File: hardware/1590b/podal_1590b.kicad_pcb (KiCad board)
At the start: 2 copper layers, 54 x 60 mm, 52 parts, among them J3 fsw pin 2, J4 fsw pin 4, J5 fsw pin 5, J8 Right out, J9 fsw pin 3, SW1 Switch 1, SW2 Switch 2, SW3 RotaryEncoder_Switch, U1 TL074, U2 L78L05_TO92

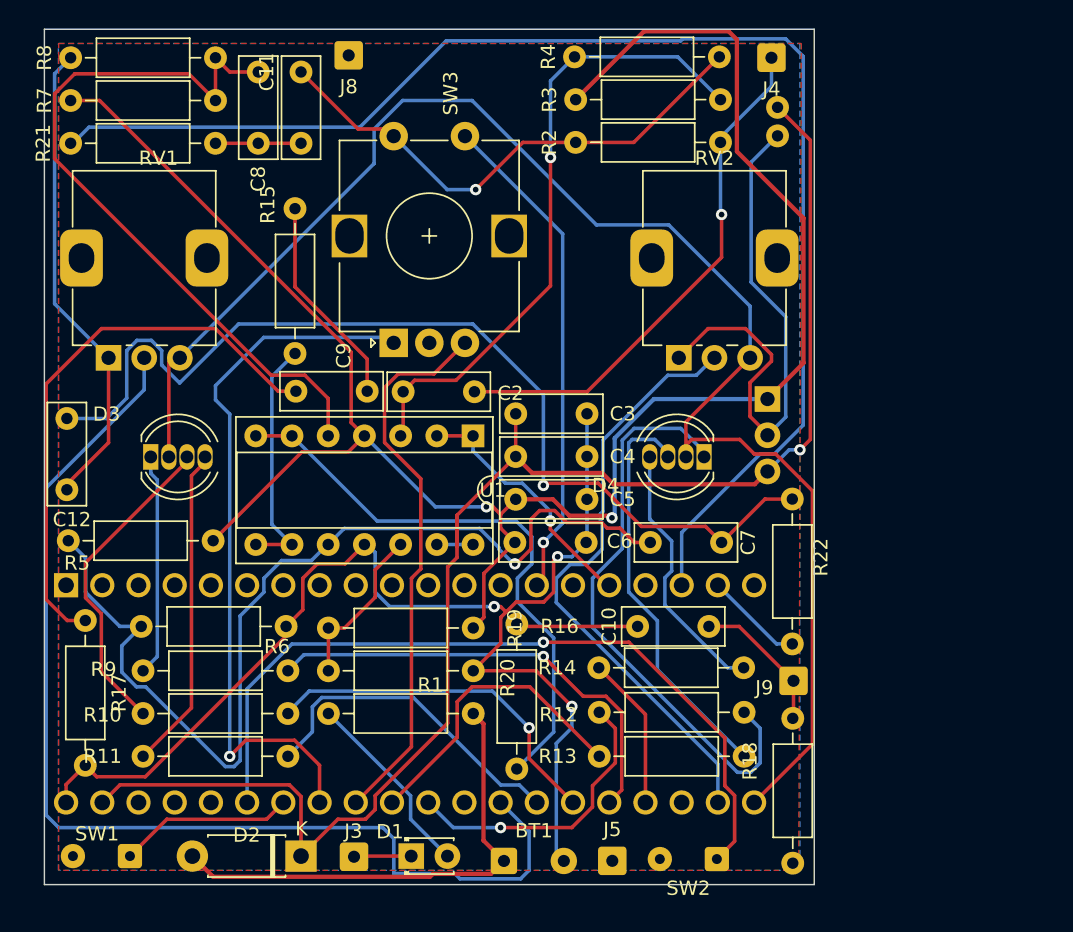
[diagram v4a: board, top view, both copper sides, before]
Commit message: Reorganise hardware into enclosure size
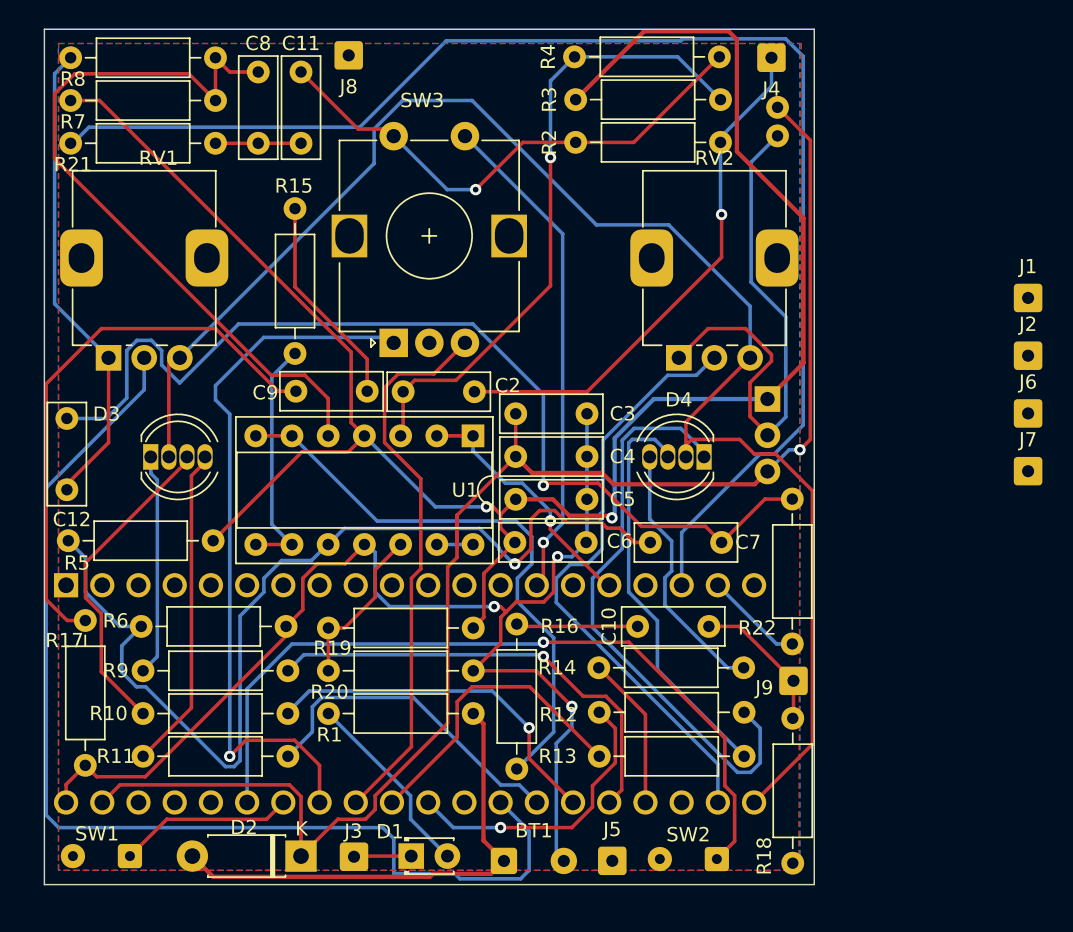
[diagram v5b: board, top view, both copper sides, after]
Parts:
- added J1: Guitar in, Connector_Wire:SolderWire-0.25sqmm_1x01_D0.65mm_OD2mm, F.Cu at (169.0, 68.8)
- added J2: fsw pin 1, Connector_Wire:SolderWire-0.25sqmm_1x01_D0.65mm_OD2mm, F.Cu at (169.0, 72.9)
- added J6: fsw pin 6, Connector_Wire:SolderWire-0.25sqmm_1x01_D0.65mm_OD2mm, F.Cu at (169.0, 77.0)
- added J7: Left out, Connector_Wire:SolderWire-0.25sqmm_1x01_D0.65mm_OD2mm, F.Cu at (169.0, 81.0)

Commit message: Tidy up pcb and compressor
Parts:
- removed J1: Guitar in, Connector_Wire:SolderWire-0.25sqmm_1x01_D0.65mm_OD2mm
- removed J2: fsw pin 1, Connector_Wire:SolderWire-0.25sqmm_1x01_D0.65mm_OD2mm
- removed J6: fsw pin 6, Connector_Wire:SolderWire-0.25sqmm_1x01_D0.65mm_OD2mm
- removed J7: Left out, Connector_Wire:SolderWire-0.25sqmm_1x01_D0.65mm_OD2mm
- moved C10 0.24 mm to (141.8, 91.7)
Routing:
- net /VCC: track 106.6 -> 104.4 mm
- net Net-(D4-RK): track 41.4 -> 42.8 mm
- net Net-(U1B-+): track 52.4 -> 53.1 mm
- net Net-(U1C-+): track 71.4 -> 72.0 mm
- net Net-(A1-ADC_0): track 42.5 -> 43.1 mm
- net Net-(D4-GK): track 28.9 -> 29.4 mm
- net Net-(A1-SAI2_SD_A): track 51.5 -> 52.0 mm

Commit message: Add footprint for the LM7805
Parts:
- U2: footprint Package_TO_SOT_THT:TO-92_Inline_Wide_78L05_dc -> Library:TO-92_Inline_Wide_78L05_dc
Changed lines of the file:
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@@
 		)
 	)
-	(footprint "Package_TO_SOT_THT:TO-92_Inline_Wide_78L05_dc"
+	(footprint "Library:TO-92_Inline_Wide_78L05_dc"
 		(layer "B.Cu")
 		(at 150.720433 75.940131 -90)
@@
 		(tags "to-92 sc-43 sc-43a sot54 PA33 transistor")
 		(property "Reference" "U2"
-			(at -0.440131 -2.279567 90)
+			(at 2.54 3.56 -90)
 			(layer "B.SilkS")
 			(effects
@@
 		)
 		(property "Value" "L78L05_TO92"
-			(at 2.54 -2.79 90)
+			(at 2.54 -2.79 -90)
 			(layer "B.Fab")
 			(effects
@@
 			)
 		)
-		(property "Footprint" "Package_TO_SOT_THT:TO-92_Inline_Wide_78L05_dc"
-			(at 0 0 -90)
+		(property "Footprint" "Library:TO-92_Inline_Wide_78L05_dc"
+			(at 0 0 90)
 			(unlocked yes)
-			(layer "F.Fab")
+			(layer "B.Fab")
 			(hide yes)
 			(effects
@@
 					(size 1.27 1.27)
 				)
+				(justify mirror)
 			)
 		)
 		(property "Datasheet" "http://www.st.com/content/ccc/resource/technical/document/datasheet/15/55/e5/aa/23/5b/43/fd/CD00000446.pdf/files/CD00000446.pdf/jcr:content/translations/en.CD00000446.pdf"
-			(at 0 0 -90)
+			(at 0 0 90)
 			(unlocked yes)
-			(layer "F.Fab")
+			(layer "B.Fab")
 			(hide yes)
 			(effects
@@
 					(size 1.27 1.27)
 				)
+				(justify mirror)
 			)
 		)
 		(property "Description" ""
-			(at 0 0 -90)
+			(at 0 0 90)
 			(unlocked yes)
-			(layer "F.Fab")
+			(layer "B.Fab")
 			(hide yes)
 			(effects
@@
 					(size 1.27 1.27)
 				)
+				(justify mirror)
 			)
 		)
@@
 		(attr through_hole)
 		(fp_line
-			(start 0.74 -1.85)
-			(end 4.34 -1.85)
+			(start 4.34 -1.85)
+			(end 0.74 -1.85)
 			(stroke
 				(width 0.12)
@@
 		)
 		(fp_line
-			(start -1.01 2.73)
-			(end 6.09 2.73)
+			(start 6.09 2.73)
+			(end -1.01 2.73)
 			(stroke
 				(width 0.05)
@@
 		)
 		(fp_line
-			(start -1.01 2.73)
-			(end -1.01 -2.01)
+			(start 6.09 2.73)
+			(end 6.09 -2.01)
 			(stroke
 				(width 0.05)
@@
 		)
 		(fp_line
-			(start 6.09 -2.01)
-			(end 6.09 2.73)
+			(start -1.01 -2.01)
+			(end -1.01 2.73)
 			(stroke
 				(width 0.05)
@@
 		)
 		(fp_line
-			(start 6.09 -2.01)
-			(end -1.01 -2.01)
+			(start -1.01 -2.01)
+			(end 6.09 -2.01)
 			(stroke
 				(width 0.05)
@@
 		)
 		(fp_line
-			(start 0.8 -1.75)
-			(end 4.3 -1.75)
+			(start 4.3 -1.75)
+			(end 0.8 -1.75)
 			(stroke
 				(width 0.1)
@@
 		)
 		(fp_text user "${REFERENCE}"
-			(at 2.54 0 90)
+			(at 2.54 0 -90)
 			(layer "B.Fab")
 			(effects

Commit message: Fix Red and blue LEDs - were the wrong way round
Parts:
- added J1: Guitar in, Connector_Wire:SolderWire-0.25sqmm_1x01_D0.65mm_OD2mm, F.Cu at (1.77, 1.52)
- added J2: fsw pin 1, Connector_Wire:SolderWire-0.25sqmm_1x01_D0.65mm_OD2mm, F.Cu at (1.77, 5.58)
- added J6: fsw pin 6, Connector_Wire:SolderWire-0.25sqmm_1x01_D0.65mm_OD2mm, F.Cu at (1.77, 9.62)
- added J7: Left out, Connector_Wire:SolderWire-0.25sqmm_1x01_D0.65mm_OD2mm, F.Cu at (1.77, 13.7)
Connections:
- R11 pad 1: /LED_1_R -> /LED_1_B
- R12 pad 1: /LED_2_B -> /LED_2_R
- R14 pad 1: /LED_2_R -> /LED_2_B
- R9 pad 1: /LED_1_B -> /LED_1_R
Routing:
- net /LED_2_B: track 20.6 -> 26.1 mm
- net /LED_1_B: track 32.7 -> 28.3 mm
- net /LED_2_R: track 10.8 -> 7.67 mm
- net /LED_1_R: track 23.2 -> 21.5 mm, vias 0 -> 1
- net Net-(U1B--): track 41.1 -> 42.2 mm
